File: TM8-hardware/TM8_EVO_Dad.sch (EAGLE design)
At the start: 94 parts, among them IC1 MCP73831/OT, IC2 24LCS52ST, Q2 DMP1045U, U1 ATSAMD21G-A, U2 BME680, U4 LIS3DH, U5 DMG6968U-7, Y1 32.768kHz

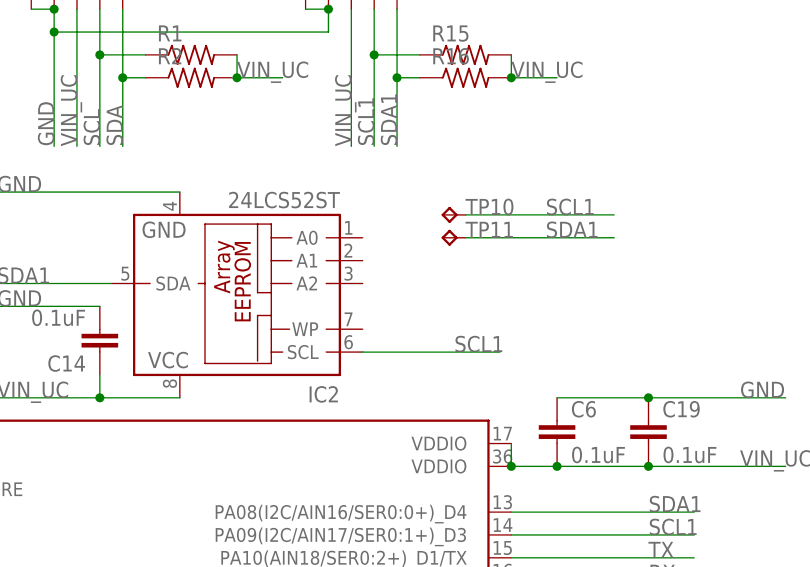
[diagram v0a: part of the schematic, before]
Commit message: made firing anim idle limit to save power
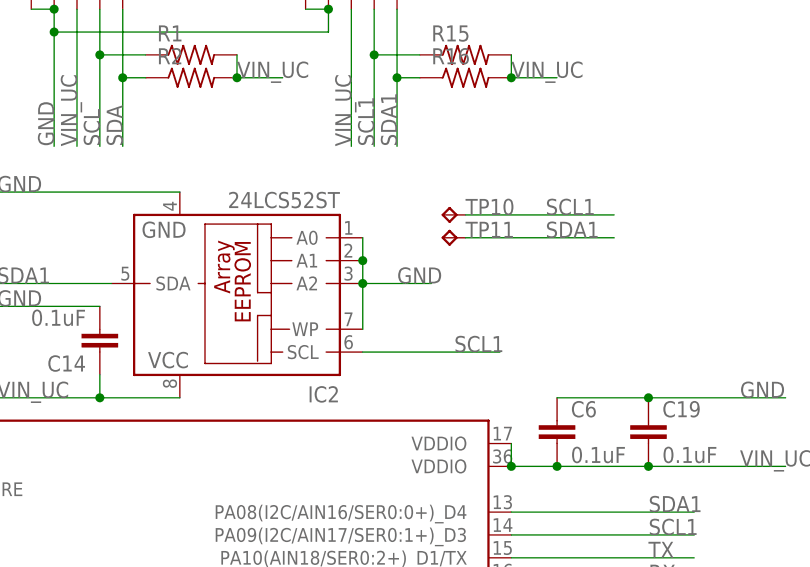
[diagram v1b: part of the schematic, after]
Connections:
- net GND: now also IC2.A0, IC2.A1, IC2.A2, IC2.WP
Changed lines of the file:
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@@
 <label x="157.48" y="116.84" size="1.778" layer="95"/>
+</segment>
+<segment>
+<pinref part="IC2" gate="G$1" pin="A2"/>
+<pinref part="IC2" gate="G$1" pin="A0"/>
+<wire x1="198.12" y1="119.38" x2="198.12" y2="121.92" width="0.1524" layer="91"/>
+<pinref part="IC2" gate="G$1" pin="A1"/>
+<wire x1="198.12" y1="121.92" x2="198.12" y2="124.46" width="0.1524" layer="91"/>
+<junction x="198.12" y="121.92"/>
+<wire x1="198.12" y1="119.38" x2="205.74" y2="119.38" width="0.1524" layer="91"/>
+<junction x="198.12" y="119.38"/>
+<label x="201.93" y="119.38" size="1.778" layer="95"/>
+<pinref part="IC2" gate="G$1" pin="WP"/>
+<wire x1="198.12" y1="114.3" x2="198.12" y2="119.38" width="0.1524" layer="91"/>
 </segment>
 </net>
